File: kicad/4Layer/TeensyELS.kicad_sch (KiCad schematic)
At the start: 43 parts, among them J1 RJ45_Shielded, J2 Conn_01x04_Pin, J3 Conn_01x04_Pin, J4 Screw_Terminal_01x02, Q1 BSS138, Q2 BSS138, Q3 BSS138, Q4 BSS138, Q5 BSS138, Q6 BSS138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

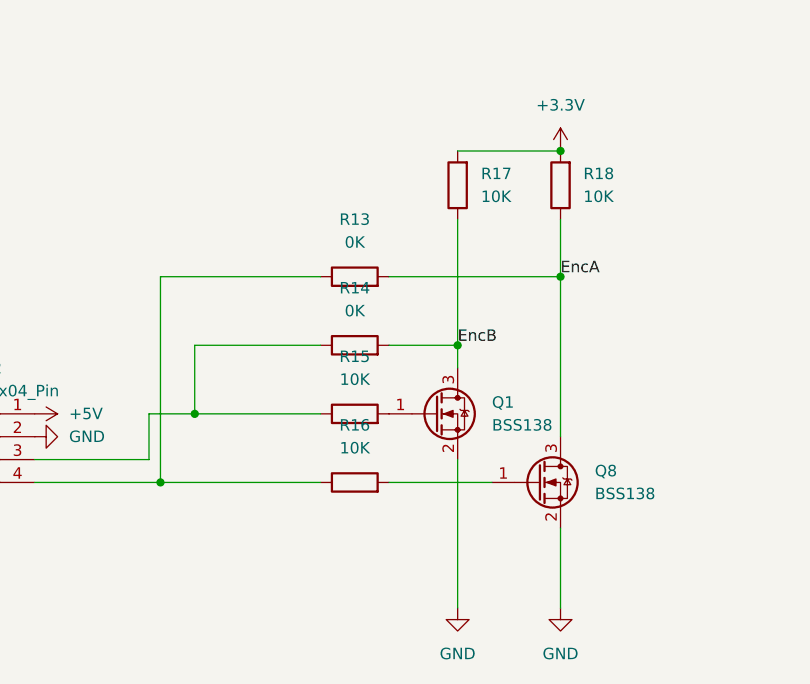
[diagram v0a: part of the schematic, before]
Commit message: Updated board design to fix incorrect pin usage
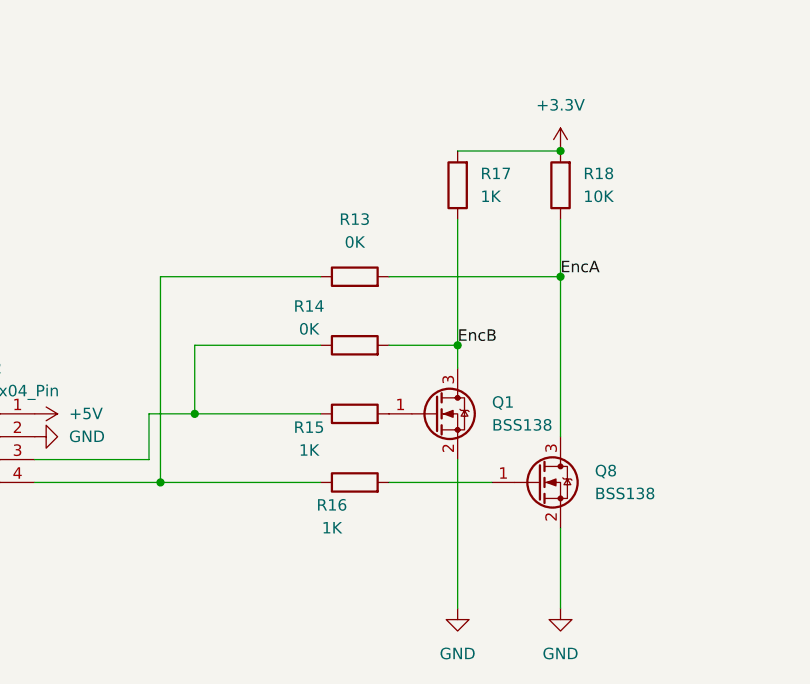
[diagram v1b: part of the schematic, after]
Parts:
- R15, R16, R17: value 10K -> 1K
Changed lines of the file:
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@@
 		(on_board yes)
 		(dnp no)
-		(fields_autoplaced yes)
 		(property "Reference" "R16"
-			(at 92.71 219.71 90)
+			(at 90.17 228.6 90)
 			(effects
 				(font
@@
 			)
 		)
-		(property "Value" "10K"
-			(at 92.71 222.25 90)
+		(property "Value" "1K"
+			(at 90.17 231.14 90)
 			(effects
 				(font
@@
 		(on_board yes)
 		(dnp no)
-		(fields_autoplaced yes)
 		(property "Reference" "R14"
-			(at 92.71 204.47 90)
+			(at 87.63 206.502 90)
 			(effects
 				(font
@@
 		)
 		(property "Value" "0K"
-			(at 92.71 207.01 90)
+			(at 87.63 209.042 90)
 			(effects
 				(font
@@
 		(fields_autoplaced yes)
 		(property "Reference" "R17"
-			(at 106.7281 191.7699 0)
+			(at 106.68 191.7699 0)
 			(effects
 				(font
@@
 			)
 		)
-		(property "Value" "10K"
-			(at 106.7281 194.3099 0)
+		(property "Value" "1K"
+			(at 106.68 194.3099 0)
 			(effects
 				(font
@@
 		(on_board yes)
 		(dnp no)
-		(fields_autoplaced yes)
 		(property "Reference" "R15"
-			(at 92.71 212.09 90)
+			(at 87.63 219.964 90)
 			(effects
 				(font
@@
 			)
 		)
-		(property "Value" "10K"
-			(at 92.71 214.63 90)
+		(property "Value" "1K"
+			(at 87.63 222.504 90)
 			(effects
 				(font
